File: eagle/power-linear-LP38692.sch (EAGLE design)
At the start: 7 parts, among them U1 LP38692

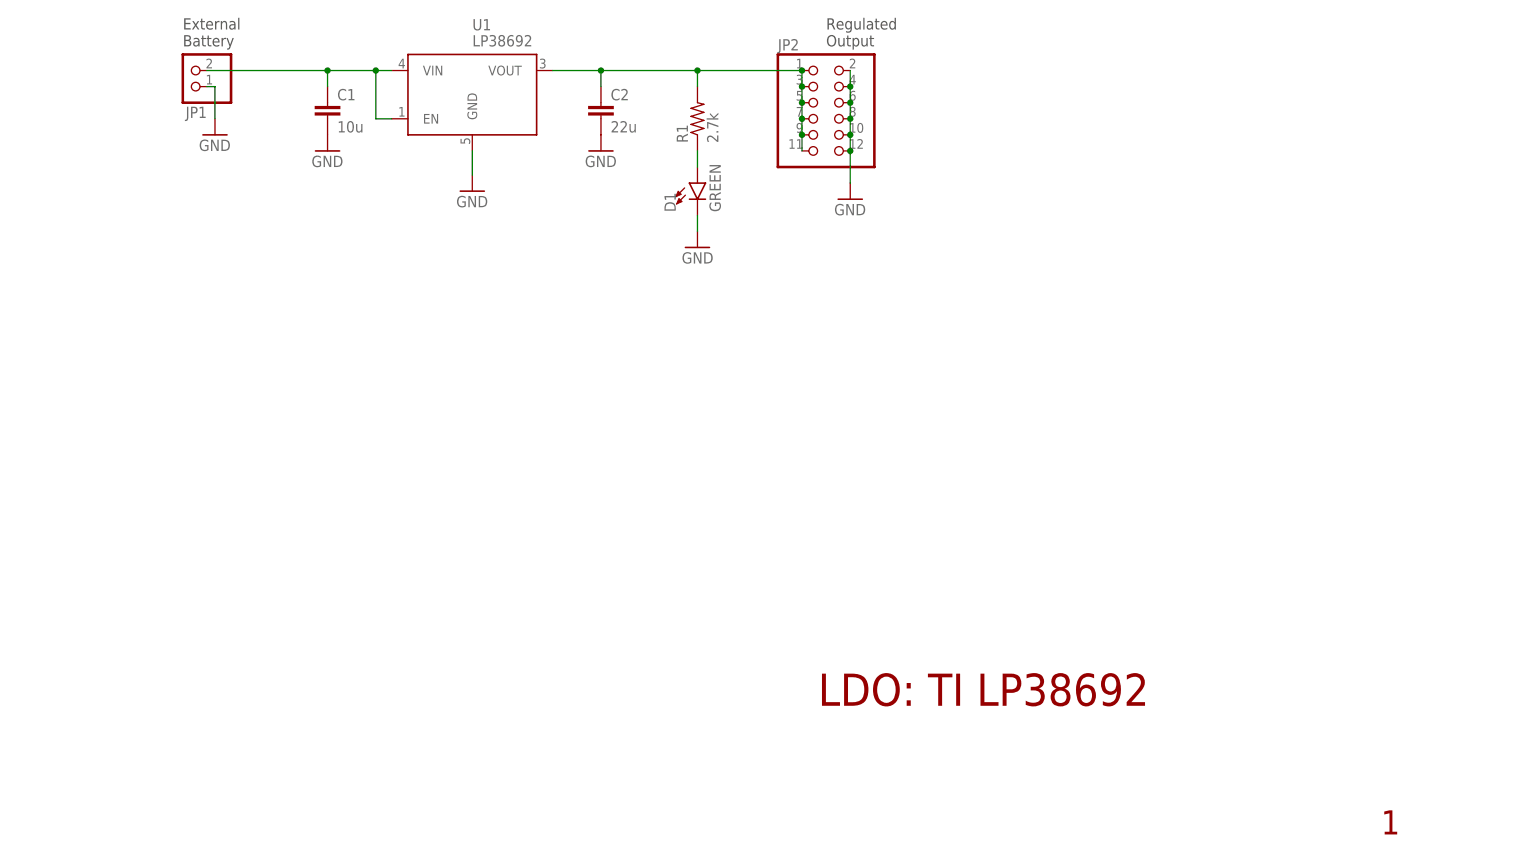
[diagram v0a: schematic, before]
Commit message: Added enable control, and sync options for switching
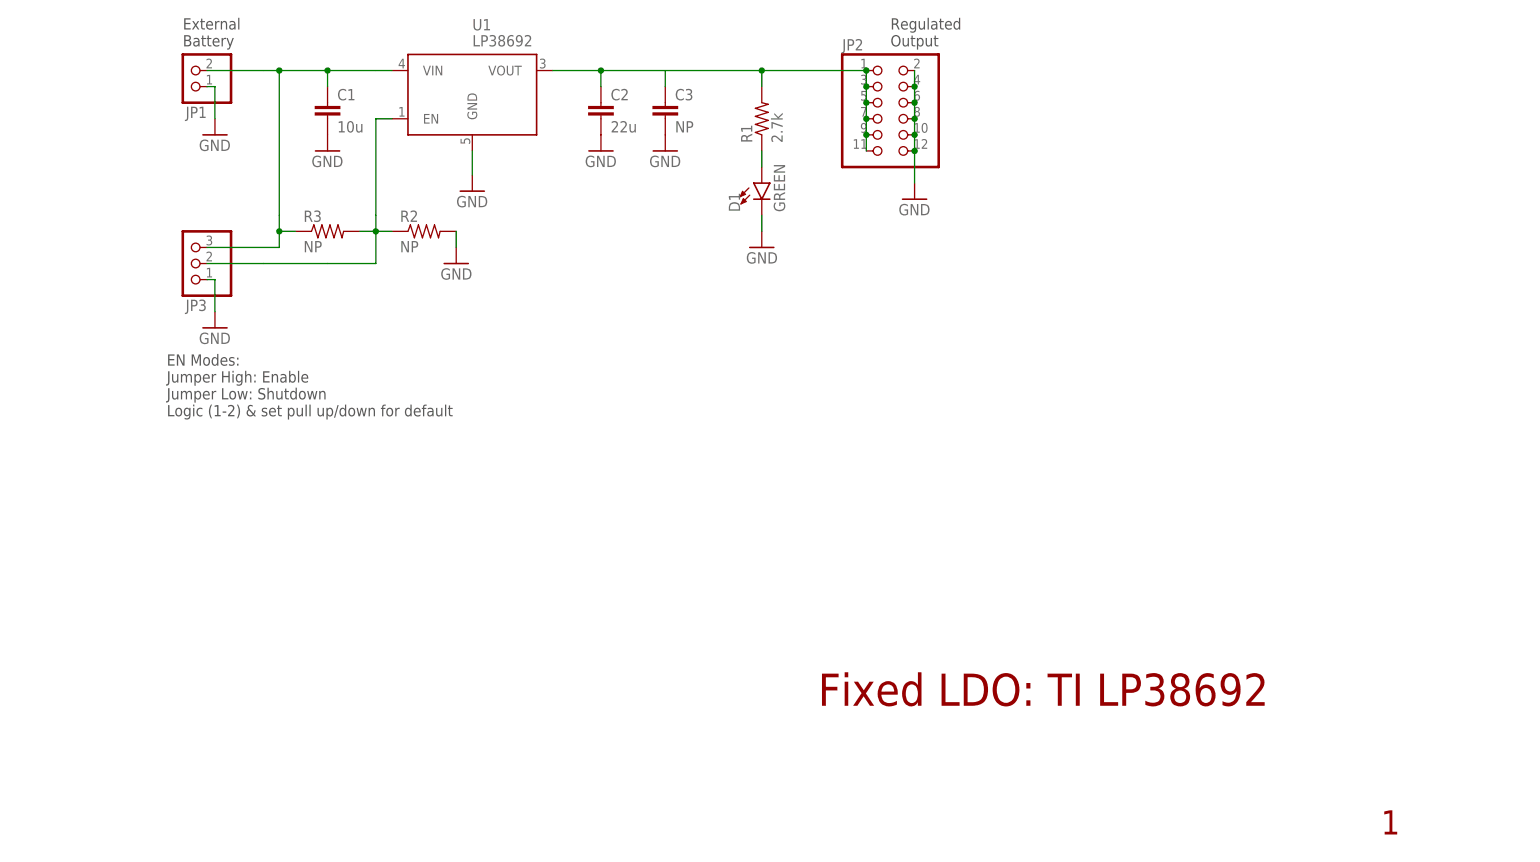
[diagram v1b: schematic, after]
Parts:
- added C3: NP, oresat-rcl:C-EU0805-B-NOSILK
- added JP3: (no value), pinhead:PINHD-1X3
- added R2, R3: NP, oresat-rcl:R-US_0603-B-NOSILK
- C2: device oresat-rcl:C-EU0603-B-NOSILK -> oresat-rcl:C-EU0805-B-NOSILK
- R1: device rcl_custom:R-US_0402-B-NOSILK -> oresat-rcl:R-US_0603-B-NOSILK; DIS Digi-Key -> (none); DPN 1276-4275-1-ND -> (none); MFR Samsung -> (none); MPN RC1005F6653CS -> (none)
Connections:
- new net N$1: C3.1
- new net N$2: JP3.2, R2.1, R3.2, U1.EN
- net GND: now also C3.2, JP3.1, R2.2
- net N$77: now also JP3.3, R3.1; no longer U1.EN
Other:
- note added: "EN Modes: Jumper High: Enable Jumper Low: Shutdown Logic (1-2) & set pull up/down for default"
- note added: "Fixed LDO: TI LP38692"
- note removed: "LDO: TI LP38692"
- moved on the sheet: D1, JP2, R1

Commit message: Finish layout
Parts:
- added D2: GREEN, SparkFun-LED:LED-GREEN0603
- added R4: NP, oresat-rcl:R-US_0603-B-NOSILK
- C1: device oresat-rcl:C-EU0603-B-NOSILK -> oresat-rcl:C-EU0805-B-NOSILK
- R1: value 2.7k -> 5.6k
- R2: value NP -> 2.7k
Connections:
- removed net N$1: C3.1
- removed net N$77: C1.1, JP1.2, JP3.3, R3.1, U1.VIN
- removed net N$89: C2.1, JP2.1, JP2.11, JP2.3, JP2.5, JP2.7, JP2.9, R1.2, U1.VOUT
- new net +VBAT: C1.1, JP1.2, JP3.3, R1.2, R3.1, U1.VIN
- new net +VOUT: C2.1, C3.1, JP2.1, JP2.11, JP2.3, JP2.5, JP2.7, JP2.9, R2.2, U1.VOUT
- new net N$78: D2.A, R2.1
- net GND: now also D2.C, R4.2; no longer R2.2
- net N$2: now also R4.1; no longer R2.1
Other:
- note added: "LED Current designed for 0.5mA Current values assume 4.5V / 3.3V (Vin/out)"
- moved on the sheet: D1, JP1, R1, R2

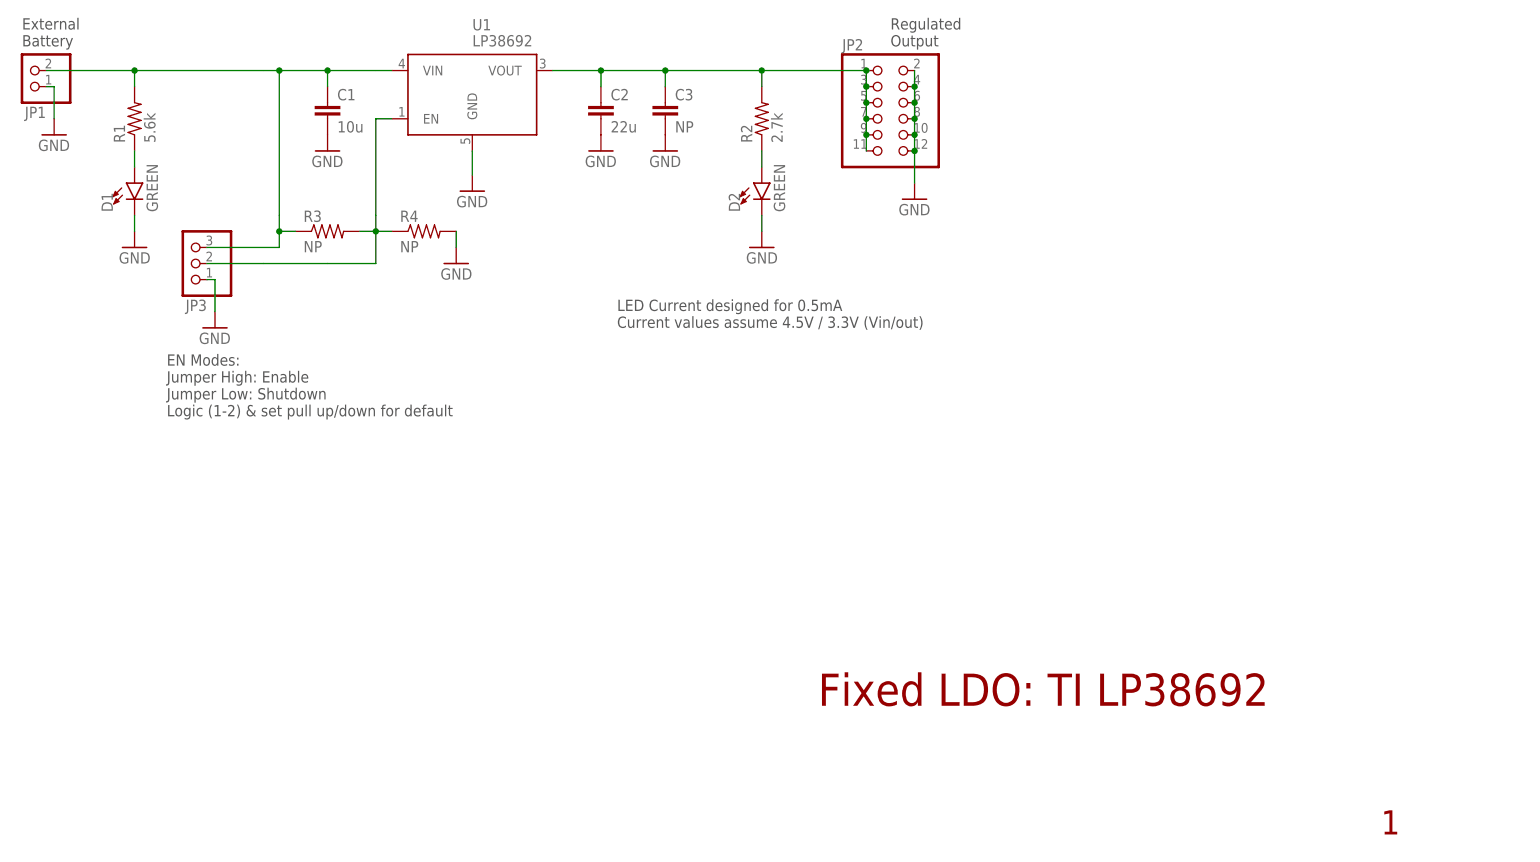
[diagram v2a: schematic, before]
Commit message: Add adjust for LP38692
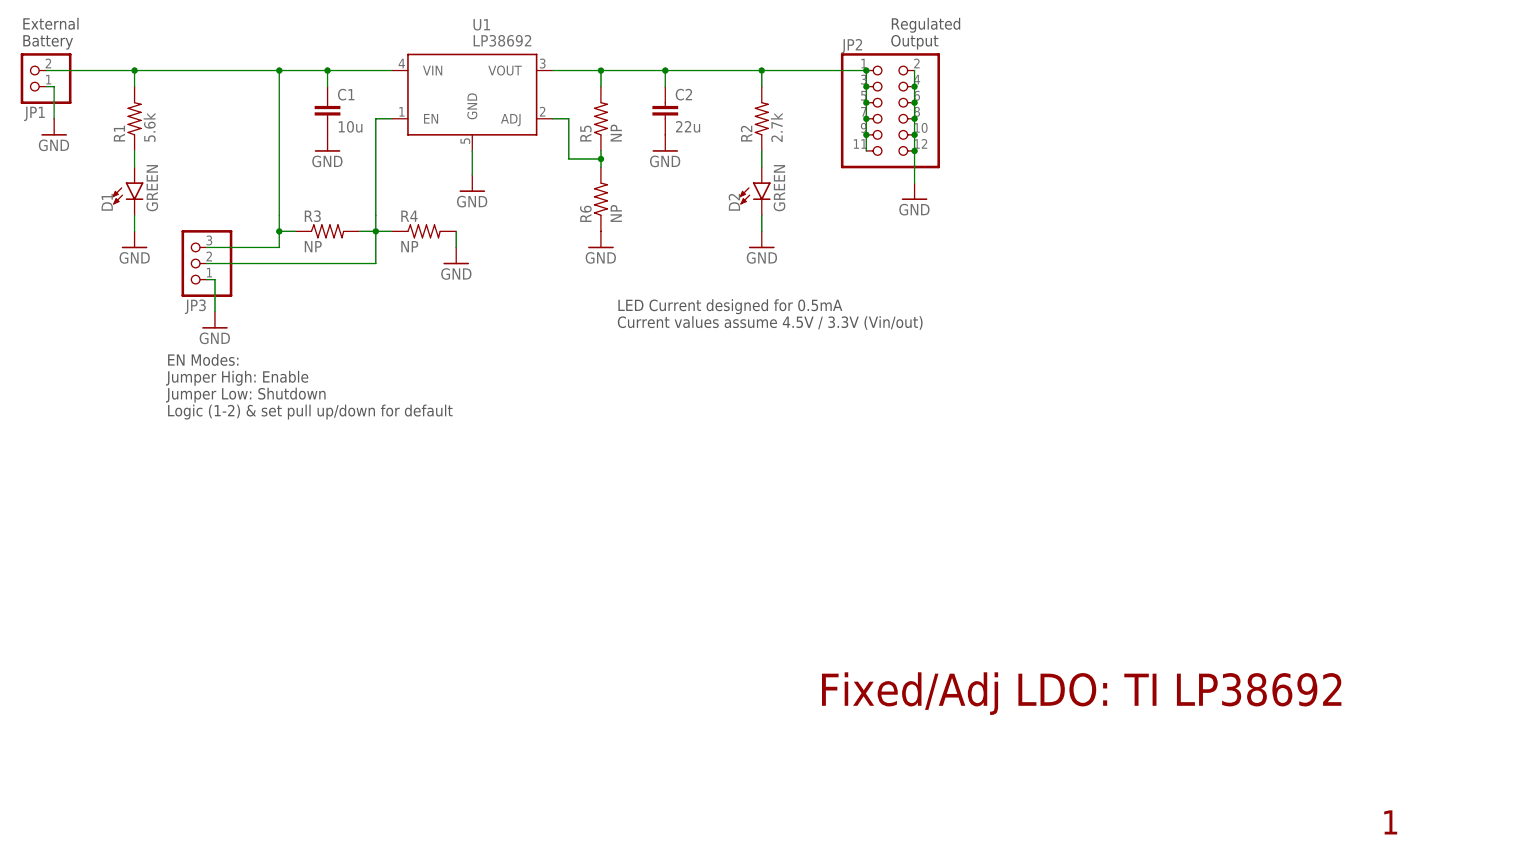
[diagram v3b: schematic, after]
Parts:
- removed C3: NP, oresat-rcl:C-EU0805-B-NOSILK
- added R5, R6: NP, oresat-rcl:R-US_0402-B-NOSILK
- C2: device oresat-rcl:C-EU0805-B-NOSILK -> oresat-rcl:C-EU1206-B
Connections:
- new net N$1: R5.1, R6.2, U1.ADJ
- net +VOUT: now also R5.2; no longer C3.1
- net GND: now also R6.1; no longer C3.2
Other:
- note added: "Fixed/Adj LDO: TI LP38692"
- note removed: "Fixed LDO: TI LP38692"
- moved on the sheet: C2
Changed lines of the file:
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@@
 <part name="JP1" library="pinhead" library_urn="urn:adsk.eagle:library:325" deviceset="PINHD-1X2" device="" package3d_urn="urn:adsk.eagle:package:22435/2"/>
 <part name="JP2" library="pinhead" library_urn="urn:adsk.eagle:library:325" deviceset="PINHD-2X6" device="" package3d_urn="urn:adsk.eagle:package:22474/2"/>
-<part name="C2" library="oresat-rcl" deviceset="C-EU" device="0805-B-NOSILK" value="22u"/>
+<part name="C2" library="oresat-rcl" deviceset="C-EU" device="1206-B" value="22u"/>
 <part name="C1" library="oresat-rcl" deviceset="C-EU" device="0805-B-NOSILK" value="10u"/>
 <part name="GND87" library="supply1" library_urn="urn:adsk.eagle:library:371" deviceset="GND" device=""/>
@@
 </part>
 <part name="GND80" library="supply1" deviceset="GND" device=""/>
-<part name="C3" library="oresat-rcl" deviceset="C-EU" device="0805-B-NOSILK" value="NP"/>
-<part name="GND1" library="supply1" library_urn="urn:adsk.eagle:library:371" deviceset="GND" device=""/>
 <part name="R2" library="oresat-rcl" deviceset="R-US_" device="0603-B-NOSILK" value="2.7k"/>
 <part name="JP3" library="pinhead" library_urn="urn:adsk.eagle:library:325" deviceset="PINHD-1X3" device="" package3d_urn="urn:adsk.eagle:package:22458/2"/>
@@
 <part name="GND5" library="supply1" deviceset="GND" device=""/>
 <part name="R1" library="oresat-rcl" deviceset="R-US_" device="0603-B-NOSILK" value="5.6k"/>
+<part name="R5" library="oresat-rcl" deviceset="R-US_" device="0402-B-NOSILK" value="NP"/>
+<part name="R6" library="oresat-rcl" deviceset="R-US_" device="0402-B-NOSILK" value="NP"/>
+<part name="GND1" library="supply1" library_urn="urn:adsk.eagle:library:371" deviceset="GND" device=""/>
 </parts>
 <sheets>
 <sheet>
 <plain>
-<text x="176.53" y="26.67" size="5.08" layer="94">Fixed LDO: TI LP38692</text>
+<text x="176.53" y="26.67" size="5.08" layer="94">Fixed/Adj LDO: TI LP38692</text>
 <text x="265.43" y="6.35" size="3.81" layer="94">1</text>
 <text x="50.8" y="130.81" size="1.778" layer="97">External
@@
 <attribute name="VALUE" x="180.34" y="109.22" size="1.778" layer="96"/>
 </instance>
-<instance part="C2" gate="CE" x="142.24" y="121.92" smashed="yes">
-<attribute name="NAME" x="143.764" y="122.301" size="1.778" layer="95"/>
-<attribute name="VALUE" x="143.764" y="117.221" size="1.778" layer="96"/>
+<instance part="C2" gate="CE" x="152.4" y="121.92" smashed="yes">
+<attribute name="NAME" x="153.924" y="122.301" size="1.778" layer="95"/>
+<attribute name="VALUE" x="153.924" y="117.221" size="1.778" layer="96"/>
 </instance>
 <instance part="C1" gate="CE" x="99.06" y="121.92" smashed="yes">
@@
 <attribute name="VALUE" x="100.584" y="117.221" size="1.778" layer="96"/>
 </instance>
-<instance part="GND87" gate="1" x="142.24" y="114.3" smashed="yes">
-<attribute name="VALUE" x="139.7" y="111.76" size="1.778" layer="96"/>
+<instance part="GND87" gate="1" x="152.4" y="114.3" smashed="yes">
+<attribute name="VALUE" x="149.86" y="111.76" size="1.778" layer="96"/>
 </instance>
 <instance part="GND89" gate="1" x="191.77" y="106.68" smashed="yes">
@@
 <attribute name="VALUE" x="170.18" y="96.52" size="1.778" layer="96" rot="MR0"/>
 </instance>
-<instance part="C3" gate="CE" x="152.4" y="121.92" smashed="yes">
-<attribute name="NAME" x="153.924" y="122.301" size="1.778" layer="95"/>
-<attribute name="VALUE" x="153.924" y="117.221" size="1.778" layer="96"/>
-</instance>
-<instance part="GND1" gate="1" x="152.4" y="114.3" smashed="yes">
-<attribute name="VALUE" x="149.86" y="111.76" size="1.778" layer="96"/>
-</instance>
 <instance part="R2" gate="R" x="167.64" y="119.38" smashed="yes" rot="R90">
 <attribute name="NAME" x="166.1414" y="115.57" size="1.778" layer="95" rot="R90"/>
@@
 <attribute name="NAME" x="67.0814" y="115.57" size="1.778" layer="95" rot="R90"/>
 <attribute name="VALUE" x="71.882" y="115.57" size="1.778" layer="96" rot="R90"/>
+</instance>
+<instance part="R5" gate="R" x="142.24" y="119.38" smashed="yes" rot="R90">
+<attribute name="NAME" x="140.7414" y="115.57" size="1.778" layer="95" rot="R90"/>
+<attribute name="VALUE" x="145.542" y="115.57" size="1.778" layer="96" rot="R90"/>
+</instance>
+<instance part="R6" gate="R" x="142.24" y="106.68" smashed="yes" rot="R90">
+<attribute name="NAME" x="140.7414" y="102.87" size="1.778" layer="95" rot="R90"/>
+<attribute name="VALUE" x="145.542" y="102.87" size="1.778" layer="96" rot="R90"/>
+</instance>
+<instance part="GND1" gate="1" x="142.24" y="99.06" smashed="yes">
+<attribute name="VALUE" x="139.7" y="96.52" size="1.778" layer="96"/>
 </instance>
 </instances>
@@
 </segment>
 <segment>
-<pinref part="C3" gate="CE" pin="2"/>
-<pinref part="GND1" gate="1" pin="GND"/>
-</segment>
-<segment>
 <pinref part="JP3" gate="A" pin="1"/>
 <pinref part="GND2" gate="1" pin="GND"/>
@@
 <pinref part="GND5" gate="1" pin="GND"/>
 <wire x1="68.58" y1="104.14" x2="68.58" y2="101.6" width="0.1524" layer="91"/>
+</segment>
+<segment>
+<pinref part="R6" gate="R" pin="1"/>
+<pinref part="GND1" gate="1" pin="GND"/>
 </segment>
 </net>
@@
 <segment>
 <pinref part="C2" gate="CE" pin="1"/>
-<wire x1="142.24" y1="124.46" x2="142.24" y2="127" width="0.1524" layer="91"/>
+<wire x1="152.4" y1="124.46" x2="152.4" y2="127" width="0.1524" layer="91"/>
 <wire x1="134.62" y1="127" x2="142.24" y2="127" width="0.1524" layer="91"/>
 <pinref part="U1" gate="G$1" pin="VOUT"/>
 <pinref part="JP2" gate="A" pin="1"/>
 <pinref part="JP2" gate="A" pin="3"/>
+<wire x1="142.24" y1="127" x2="152.4" y2="127" width="0.1524" layer="91"/>
 <wire x1="184.15" y1="127" x2="184.15" y2="124.46" width="0.1524" layer="91"/>
 <pinref part="JP2" gate="A" pin="5"/>
@@
 <wire x1="184.15" y1="116.84" x2="184.15" y2="114.3" width="0.1524" layer="91"/>
 <junction x="184.15" y="116.84"/>
-<wire x1="142.24" y1="127" x2="152.4" y2="127" width="0.1524" layer="91"/>
-<junction x="142.24" y="127"/>
+<junction x="152.4" y="127"/>
 <junction x="184.15" y="127"/>
 <wire x1="152.4" y1="127" x2="167.64" y2="127" width="0.1524" layer="91"/>
@@
 <junction x="167.64" y="127"/>
 <pinref part="R2" gate="R" pin="2"/>
-<pinref part="C3" gate="CE" pin="1"/>
-<wire x1="152.4" y1="124.46" x2="152.4" y2="127" width="0.1524" layer="91"/>
-<junction x="152.4" y="127"/>
-</segment>
-</net>
+<pinref part="R5" gate="R" pin="2"/>
+<wire x1="142.24" y1="124.46" x2="142.24" y2="127" width="0.1524" layer="91"/>
+<junction x="142.24" y="127"/>
+</segment>
+</net>
+<net name="N$1" class="0">
+<segment>
+<pinref part="R5" gate="R" pin="1"/>
+<pinref part="R6" gate="R" pin="2"/>
+<wire x1="142.24" y1="114.3" x2="142.24" y2="113.03" width="0.1524" layer="91"/>
+<pinref part="U1" gate="G$1" pin="ADJ"/>
+<wire x1="142.24" y1="113.03" x2="142.24" y2="111.76" width="0.1524" layer="91"/>
+<wire x1="134.62" y1="119.38" x2="137.16" y2="119.38" width="0.1524" layer="91"/>
+<wire x1="137.16" y1="119.38" x2="137.16" y2="113.03" width="0.1524" layer="91"/>
+<wire x1="137.16" y1="113.03" x2="142.24" y2="113.03" width="0.1524" layer="91"/>
+<junction x="142.24" y="113.03"/>
+</segment>
+</net>

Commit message: Change res sizes for LP38692
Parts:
- R3, R4: device oresat-rcl:R-US_0603-B-NOSILK -> oresat-rcl:R-US_0402-B-NOSILK
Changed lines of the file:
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@@
 <part name="JP3" library="pinhead" library_urn="urn:adsk.eagle:library:325" deviceset="PINHD-1X3" device="" package3d_urn="urn:adsk.eagle:package:22458/2"/>
 <part name="GND2" library="supply1" library_urn="urn:adsk.eagle:library:371" deviceset="GND" device=""/>
-<part name="R4" library="oresat-rcl" deviceset="R-US_" device="0603-B-NOSILK" value="NP"/>
+<part name="R4" library="oresat-rcl" deviceset="R-US_" device="0402-B-NOSILK" value="NP"/>
 <part name="GND4" library="supply1" deviceset="GND" device=""/>
-<part name="R3" library="oresat-rcl" deviceset="R-US_" device="0603-B-NOSILK" value="NP"/>
+<part name="R3" library="oresat-rcl" deviceset="R-US_" device="0402-B-NOSILK" value="NP"/>
 <part name="D1" library="SparkFun-LED" library_urn="urn:adsk.eagle:library:529" deviceset="LED-GREEN" device="0603" package3d_urn="urn:adsk.eagle:package:39354/1" value="GREEN">
 <attribute name="PROD_ID" value=""/>
